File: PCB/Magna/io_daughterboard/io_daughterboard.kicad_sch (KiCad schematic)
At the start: 3 parts, among them J101 Conn_02x10_Counter_Clockwise

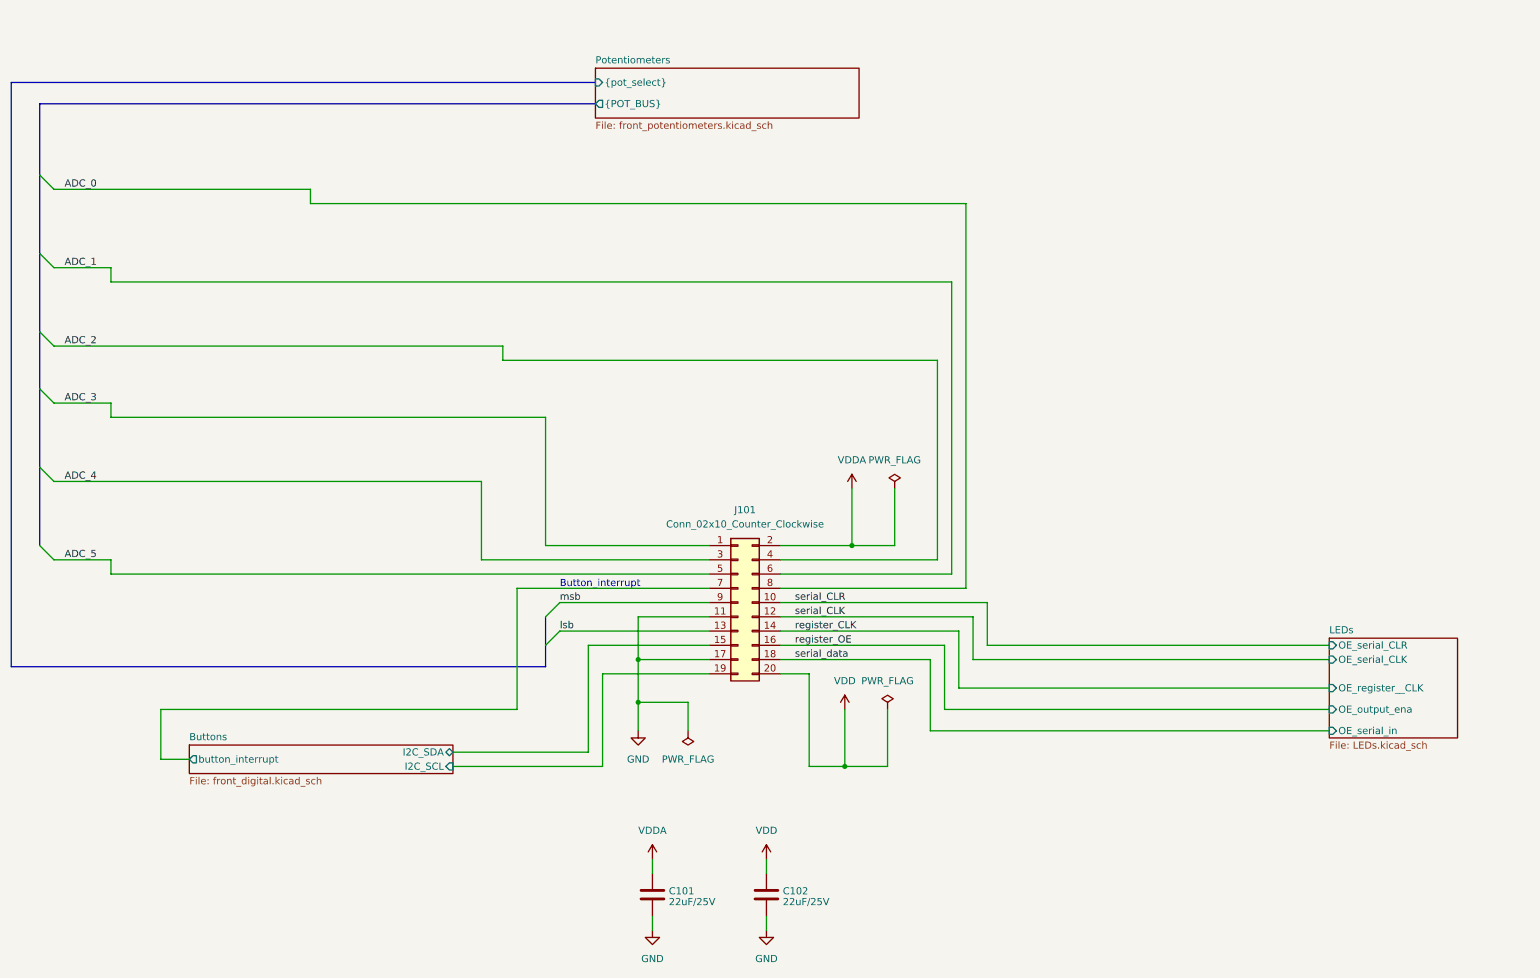
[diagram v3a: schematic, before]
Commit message: Mainboard layout (#19)
Also adds mounting holes to IO daughterboard
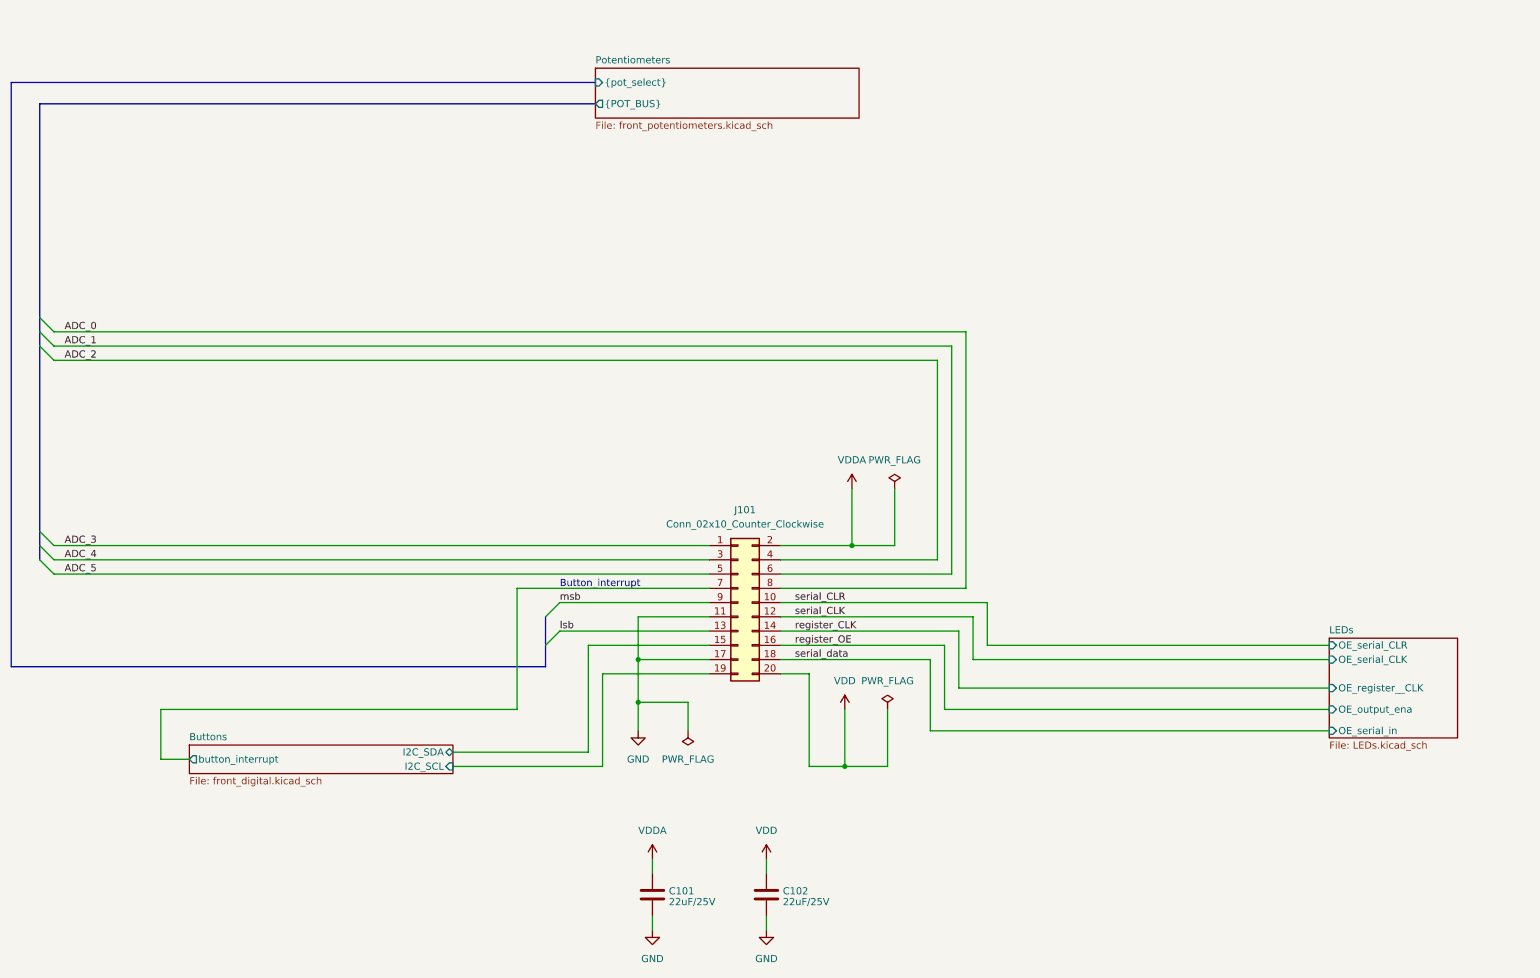
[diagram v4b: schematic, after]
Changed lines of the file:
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@@
   (junction (at 162.56 147.32) (diameter 0) (color 0 0 0 0)
   )
+  (bus_entry (at 19.05 72.39) (size 2.54 2.54)
+    (stroke (width 0) (type default))
+  )
+  (bus_entry (at 111.76 118.11) (size -2.54 2.54)
+    (stroke (width 0) (type default))
+  )
+  (bus_entry (at 19.05 107.95) (size 2.54 2.54)
+    (stroke (width 0) (type default))
+  )
+  (bus_entry (at 19.05 110.49) (size 2.54 2.54)
+    (stroke (width 0) (type default))
+  )
+  (bus_entry (at 19.05 105.41) (size 2.54 2.54)
+    (stroke (width 0) (type default))
+  )
+  (bus_entry (at 109.22 125.73) (size 2.54 -2.54)
+    (stroke (width 0) (type default))
+  )
   (bus_entry (at 19.05 69.85) (size 2.54 2.54)
     (stroke (width 0) (type default))
   )
-  (bus_entry (at 111.76 118.11) (size -2.54 2.54)
-    (stroke (width 0) (type default))
-  )
-  (bus_entry (at 19.05 93.98) (size 2.54 2.54)
-    (stroke (width 0) (type default))
-  )
-  (bus_entry (at 19.05 107.95) (size 2.54 2.54)
-    (stroke (width 0) (type default))
-  )
-  (bus_entry (at 19.05 80.01) (size 2.54 2.54)
-    (stroke (width 0) (type default))
-  )
-  (bus_entry (at 109.22 125.73) (size 2.54 -2.54)
-    (stroke (width 0) (type default))
-  )
-  (bus_entry (at 19.05 55.88) (size 2.54 2.54)
-    (stroke (width 0) (type default))
-  )
-  (bus_entry (at 19.05 41.91) (size 2.54 2.54)
+  (bus_entry (at 19.05 67.31) (size 2.54 2.54)
     (stroke (width 0) (type default))
   )
@@
     (stroke (width 0) (type default))
   )
-  (wire (pts (xy 31.75 60.96) (xy 181.61 60.96))
-    (stroke (width 0) (type default))
-  )
-  (wire (pts (xy 97.79 96.52) (xy 97.79 110.49))
-    (stroke (width 0) (type default))
-  )
-  (wire (pts (xy 31.75 85.09) (xy 31.75 82.55))
-    (stroke (width 0) (type default))
-  )
   (wire (pts (xy 40.64 146.05) (xy 40.64 137.16))
     (stroke (width 0) (type default))
   )
-  (wire (pts (xy 21.59 58.42) (xy 31.75 58.42))
-    (stroke (width 0) (type default))
-  )
-  (wire (pts (xy 21.59 96.52) (xy 97.79 96.52))
+  (wire (pts (xy 21.59 72.39) (xy 181.61 72.39))
+    (stroke (width 0) (type default))
+  )
+  (wire (pts (xy 21.59 110.49) (xy 138.43 110.49))
     (stroke (width 0) (type default))
   )
@@
     (stroke (width 0) (type default))
   )
-  (wire (pts (xy 67.31 46.99) (xy 184.15 46.99))
-    (stroke (width 0) (type default))
-  )
-  (wire (pts (xy 21.59 82.55) (xy 31.75 82.55))
-    (stroke (width 0) (type default))
-  )
   (wire (pts (xy 104.14 137.16) (xy 104.14 115.57))
     (stroke (width 0) (type default))
@@
     (stroke (width 0) (type default))
   )
-  (wire (pts (xy 67.31 44.45) (xy 67.31 46.99))
-    (stroke (width 0) (type default))
-  )
   (wire (pts (xy 125.73 135.89) (xy 134.62 135.89))
     (stroke (width 0) (type default))
   )
-  (wire (pts (xy 31.75 85.09) (xy 109.22 85.09))
-    (stroke (width 0) (type default))
-  )
-  (bus (pts (xy 19.05 80.01) (xy 19.05 93.98))
-    (stroke (width 0) (type default))
-  )
-  (bus (pts (xy 19.05 55.88) (xy 19.05 69.85))
-    (stroke (width 0) (type default))
-  )
-  (wire (pts (xy 31.75 113.03) (xy 138.43 113.03))
+  (bus (pts (xy 19.05 105.41) (xy 19.05 107.95))
+    (stroke (width 0) (type default))
+  )
+  (bus (pts (xy 19.05 69.85) (xy 19.05 72.39))
     (stroke (width 0) (type default))
   )
@@
     (stroke (width 0) (type default))
   )
-  (wire (pts (xy 21.59 110.49) (xy 31.75 110.49))
+  (wire (pts (xy 21.59 113.03) (xy 138.43 113.03))
     (stroke (width 0) (type default))
   )
@@
     (stroke (width 0) (type default))
   )
-  (wire (pts (xy 184.15 46.99) (xy 184.15 115.57))
+  (wire (pts (xy 184.15 69.85) (xy 184.15 115.57))
     (stroke (width 0) (type default))
   )
@@
     (stroke (width 0) (type default))
   )
-  (wire (pts (xy 101.6 74.93) (xy 179.07 74.93))
-    (stroke (width 0) (type default))
-  )
   (wire (pts (xy 148.59 173.99) (xy 148.59 176.53))
     (stroke (width 0) (type default))
   )
-  (wire (pts (xy 101.6 72.39) (xy 101.6 74.93))
-    (stroke (width 0) (type default))
-  )
   (wire (pts (xy 151.13 123.19) (xy 182.88 123.19))
     (stroke (width 0) (type default))
@@
     (stroke (width 0) (type default))
   )
-  (bus (pts (xy 19.05 69.85) (xy 19.05 80.01))
+  (bus (pts (xy 19.05 72.39) (xy 19.05 105.41))
     (stroke (width 0) (type default))
   )
@@
     (stroke (width 0) (type default))
   )
-  (bus (pts (xy 19.05 29.21) (xy 19.05 41.91))
-    (stroke (width 0) (type default))
-  )
-  (wire (pts (xy 181.61 60.96) (xy 181.61 113.03))
-    (stroke (width 0) (type default))
-  )
-  (wire (pts (xy 138.43 107.95) (xy 109.22 107.95))
+  (bus (pts (xy 19.05 29.21) (xy 19.05 67.31))
+    (stroke (width 0) (type default))
+  )
+  (wire (pts (xy 181.61 72.39) (xy 181.61 113.03))
+    (stroke (width 0) (type default))
+  )
+  (wire (pts (xy 21.59 107.95) (xy 138.43 107.95))
     (stroke (width 0) (type default))
   )
@@
     (stroke (width 0) (type default))
   )
-  (bus (pts (xy 19.05 93.98) (xy 19.05 107.95))
-    (stroke (width 0) (type default))
-  )
-  (wire (pts (xy 21.59 72.39) (xy 101.6 72.39))
+  (bus (pts (xy 19.05 107.95) (xy 19.05 110.49))
+    (stroke (width 0) (type default))
+  )
+  (wire (pts (xy 21.59 74.93) (xy 179.07 74.93))
     (stroke (width 0) (type default))
   )
@@
     (stroke (width 0) (type default))
   )
-  (wire (pts (xy 21.59 44.45) (xy 67.31 44.45))
-    (stroke (width 0) (type default))
-  )
-  (wire (pts (xy 97.79 110.49) (xy 138.43 110.49))
-    (stroke (width 0) (type default))
-  )
-  (wire (pts (xy 31.75 113.03) (xy 31.75 110.49))
+  (wire (pts (xy 21.59 69.85) (xy 184.15 69.85))
     (stroke (width 0) (type default))
   )
@@
     (stroke (width 0) (type default))
   )
-  (wire (pts (xy 109.22 107.95) (xy 109.22 85.09))
-    (stroke (width 0) (type default))
-  )
   (wire (pts (xy 162.56 137.16) (xy 162.56 147.32))
     (stroke (width 0) (type default))
@@
     (stroke (width 0) (type default))
   )
-  (bus (pts (xy 19.05 41.91) (xy 19.05 55.88))
+  (bus (pts (xy 19.05 67.31) (xy 19.05 69.85))
     (stroke (width 0) (type default))
   )
@@
     (stroke (width 0) (type default))
   )
-  (wire (pts (xy 31.75 60.96) (xy 31.75 58.42))
-    (stroke (width 0) (type default))
-  )
   (wire (pts (xy 156.21 147.32) (xy 156.21 130.81))
     (stroke (width 0) (type default))
@@
     (effects (font (size 1.27 1.27)) (justify left bottom))
   )
-  (label "ADC_4" (at 29.21 96.52 180) (fields_autoplaced)
-    (effects (font (size 1.27 1.27)) (justify right bottom))
-  )
-  (label "ADC_1" (at 29.21 58.42 180) (fields_autoplaced)
+  (label "ADC_4" (at 29.21 110.49 180) (fields_autoplaced)
+    (effects (font (size 1.27 1.27)) (justify right bottom))
+  )
+  (label "ADC_1" (at 29.21 72.39 180) (fields_autoplaced)
     (effects (font (size 1.27 1.27)) (justify right bottom))
   )
@@
     (effects (font (size 1.27 1.27)) (justify left bottom))
   )
-  (label "ADC_3" (at 29.21 82.55 180) (fields_autoplaced)
+  (label "ADC_3" (at 29.21 107.95 180) (fields_autoplaced)
     (effects (font (size 1.27 1.27)) (justify right bottom))
   )
@@
     (effects (font (size 1.27 1.27)) (justify left bottom))
   )
-  (label "ADC_2" (at 29.21 72.39 180) (fields_autoplaced)
-    (effects (font (size 1.27 1.27)) (justify right bottom))
-  )
-  (label "ADC_5" (at 29.21 110.49 180) (fields_autoplaced)
+  (label "ADC_2" (at 29.21 74.93 180) (fields_autoplaced)
+    (effects (font (size 1.27 1.27)) (justify right bottom))
+  )
+  (label "ADC_5" (at 29.21 113.03 180) (fields_autoplaced)
     (effects (font (size 1.27 1.27)) (justify right bottom))
   )
@@
     (effects (font (size 1.27 1.27)) (justify left bottom))
   )
-  (label "ADC_0" (at 29.21 44.45 180) (fields_autoplaced)
-    (effects (font (size 1.27 1.27)) (justify right bottom))
-  )
+  (label "ADC_0" (at 29.21 69.85 180) (fields_autoplaced)
+    (effects (font (size 1.27 1.27)) (justify right bottom))
+  )

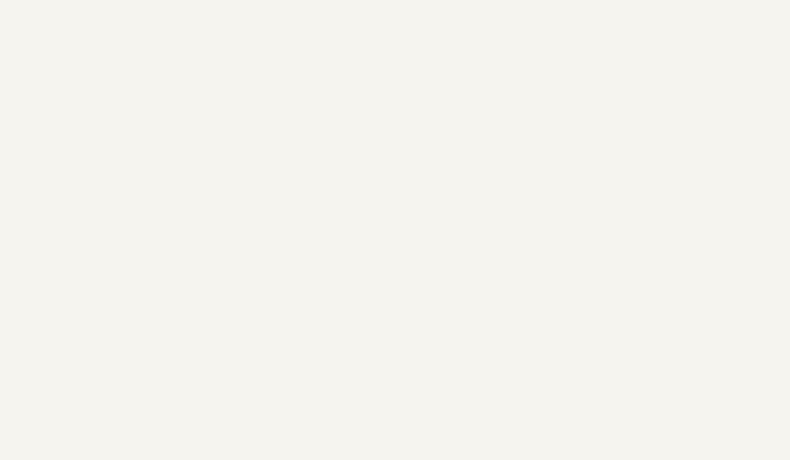
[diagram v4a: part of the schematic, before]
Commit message: Start of redesign of Audio board
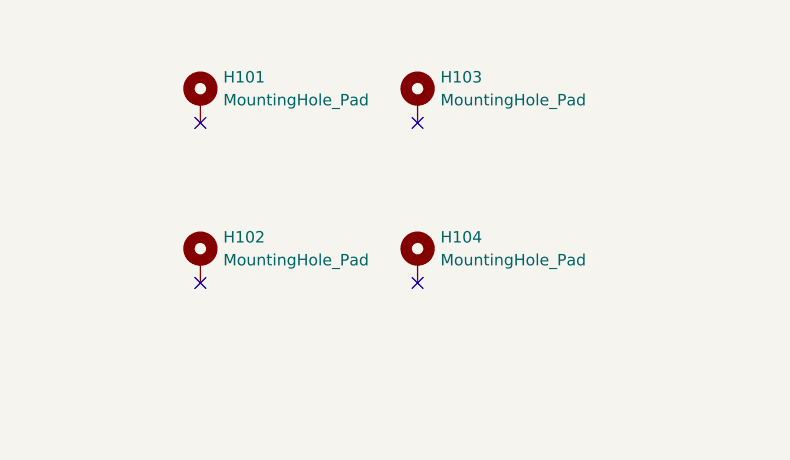
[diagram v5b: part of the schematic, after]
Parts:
- added H101, H102, H103, H104: MountingHole_Pad, MountingHole:MountingHole_3.2mm_M3_Pad_Via, symbol Mechanical:MountingHole_Pad
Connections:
- no-connect marks 0 -> 4
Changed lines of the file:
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@@
   (junction (at 162.56 147.32) (diameter 0) (color 0 0 0 0)
   )
+  (no_connect (at 233.68 31.75))
+  (no_connect (at 209.55 49.53))
+  (no_connect (at 209.55 31.75))
+  (no_connect (at 233.68 49.53))
   (bus_entry (at 19.05 72.39) (size 2.54 2.54)
     (stroke (width 0) (type default))
@@
     (effects (font (size 1.27 1.27)) (justify right bottom))
   )
+  (symbol (lib_id "Mechanical:MountingHole_Pad") (at 233.68 46.99 0) (unit 1)
+    (in_bom yes) (on_board yes) (dnp no) (fields_autoplaced)
+    (property "Reference" "H104" (at 236.22 44.45 0)
+      (effects (font (size 1.27 1.27)) (justify left))
+    )
+    (property "Value" "MountingHole_Pad" (at 236.22 46.99 0)
+      (effects (font (size 1.27 1.27)) (justify left))
+    )
+    (property "Footprint" "MountingHole:MountingHole_3.2mm_M3_Pad_Via" (at 233.68 46.99 0)
+      (effects (font (size 1.27 1.27)) hide)
+    )
+    (property "Datasheet" "~" (at 233.68 46.99 0)
+      (effects (font (size 1.27 1.27)) hide)
+    )
+    (pin "1")
+    (instances
+      (project "io_daughterboard"
+        (path "/ad211228-4c3e-4f95-b724-9dfcdf1751b2"
+          (reference "H104") (unit 1)
+        )
+      )
+    )
+  )
   (symbol (lib_id "power:GND") (at 125.73 140.97 0) (mirror y) (unit 1)
     (in_bom yes) (on_board yes) (dnp no) (fields_autoplaced)
@@
     )
   )
+  (symbol (lib_id "Mechanical:MountingHole_Pad") (at 233.68 29.21 0) (unit 1)
+    (in_bom yes) (on_board yes) (dnp no) (fields_autoplaced)
+    (property "Reference" "H103" (at 236.22 26.67 0)
+      (effects (font (size 1.27 1.27)) (justify left))
+    )
+    (property "Value" "MountingHole_Pad" (at 236.22 29.21 0)
+      (effects (font (size 1.27 1.27)) (justify left))
+    )
+    (property "Footprint" "MountingHole:MountingHole_3.2mm_M3_Pad_Via" (at 233.68 29.21 0)
+      (effects (font (size 1.27 1.27)) hide)
+    )
+    (property "Datasheet" "~" (at 233.68 29.21 0)
+      (effects (font (size 1.27 1.27)) hide)
+    )
+    (pin "1")
+    (instances
+      (project "io_daughterboard"
+        (path "/ad211228-4c3e-4f95-b724-9dfcdf1751b2"
+          (reference "H103") (unit 1)
+        )
+      )
+    )
+  )
   (symbol (lib_id "power:VDDA") (at 163.83 97.79 0) (unit 1)
     (in_bom yes) (on_board yes) (dnp no) (fields_autoplaced)
@@
         )
       )
+    )
+  )
+  (symbol (lib_id "Mechanical:MountingHole_Pad") (at 209.55 29.21 0) (unit 1)
+    (in_bom yes) (on_board yes) (dnp no) (fields_autoplaced)
+    (property "Reference" "H101" (at 212.09 26.67 0)
+      (effects (font (size 1.27 1.27)) (justify left))
+    )
+    (property "Value" "MountingHole_Pad" (at 212.09 29.21 0)
+      (effects (font (size 1.27 1.27)) (justify left))
+    )
+    (property "Footprint" "MountingHole:MountingHole_3.2mm_M3_Pad_Via" (at 209.55 29.21 0)
+      (effects (font (size 1.27 1.27)) hide)
+    )
+    (property "Datasheet" "~" (at 209.55 29.21 0)
+      (effects (font (size 1.27 1.27)) hide)
+    )
+    (pin "1")
+    (instances
+      (project "io_daughterboard"
+        (path "/ad211228-4c3e-4f95-b724-9dfcdf1751b2"
+          (reference "H101") (unit 1)
+        )
+      )
+    )
+  )
+  (symbol (lib_id "Mechanical:MountingHole_Pad") (at 209.55 46.99 0) (unit 1)
+    (in_bom yes) (on_board yes) (dnp no) (fields_autoplaced)
+    (property "Reference" "H102" (at 212.09 44.45 0)
+      (effects (font (size 1.27 1.27)) (justify left))
+    )
+    (property "Value" "MountingHole_Pad" (at 212.09 46.99 0)
+      (effects (font (size 1.27 1.27)) (justify left))
+    )
+    (property "Footprint" "MountingHole:MountingHole_3.2mm_M3_Pad_Via" (at 209.55 46.99 0)
+      (effects (font (size 1.27 1.27)) hide)
+    )
+    (property "Datasheet" "~" (at 209.55 46.99 0)
+      (effects (font (size 1.27 1.27)) hide)
+    )
+    (pin "1")
+    (instances
+      (project "io_daughterboard"
+        (path "/ad211228-4c3e-4f95-b724-9dfcdf1751b2"
+          (reference "H102") (unit 1)
+        )
+      )
